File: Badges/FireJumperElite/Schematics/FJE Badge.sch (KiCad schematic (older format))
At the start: 38 parts, among them J1 USB_C_Receptacle, J2 Prog, J3 Conn_02x03_Odd_Even, J4 Conn_02x03_Odd_Even, SW1 SW_DIP_x01, SW2 SW_DIP_x01, SW3 SW_DIP_x01, U1 TLV1117-33, U2 HX4056, U3 STM32F042F6Px

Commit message: Putting stuff together
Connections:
- net at Power->1.3 (C), R3.2: now also C2.2
- net at R3.1, U1.3 (VI): no longer C2.2
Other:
- moved on the sheet: BT1, C1, C2, C3, C4, C5, C6, C7, C8, C9, D1, D10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

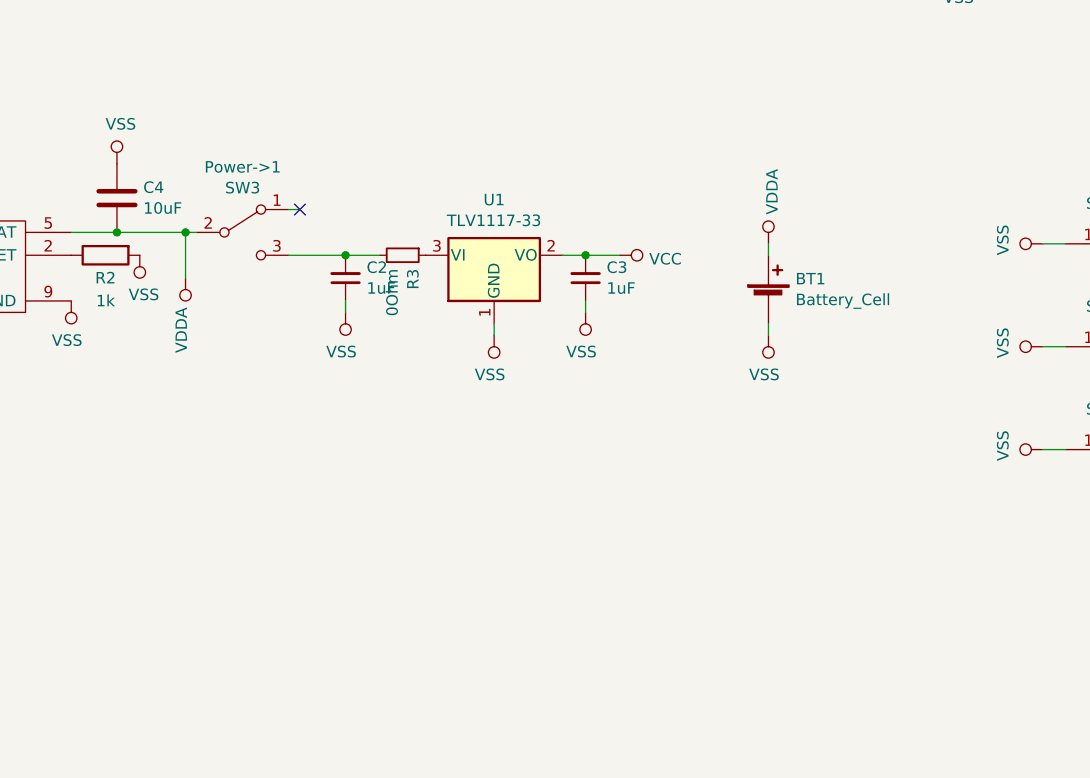
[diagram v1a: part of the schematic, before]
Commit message: FJE Badge Charlieplexing done
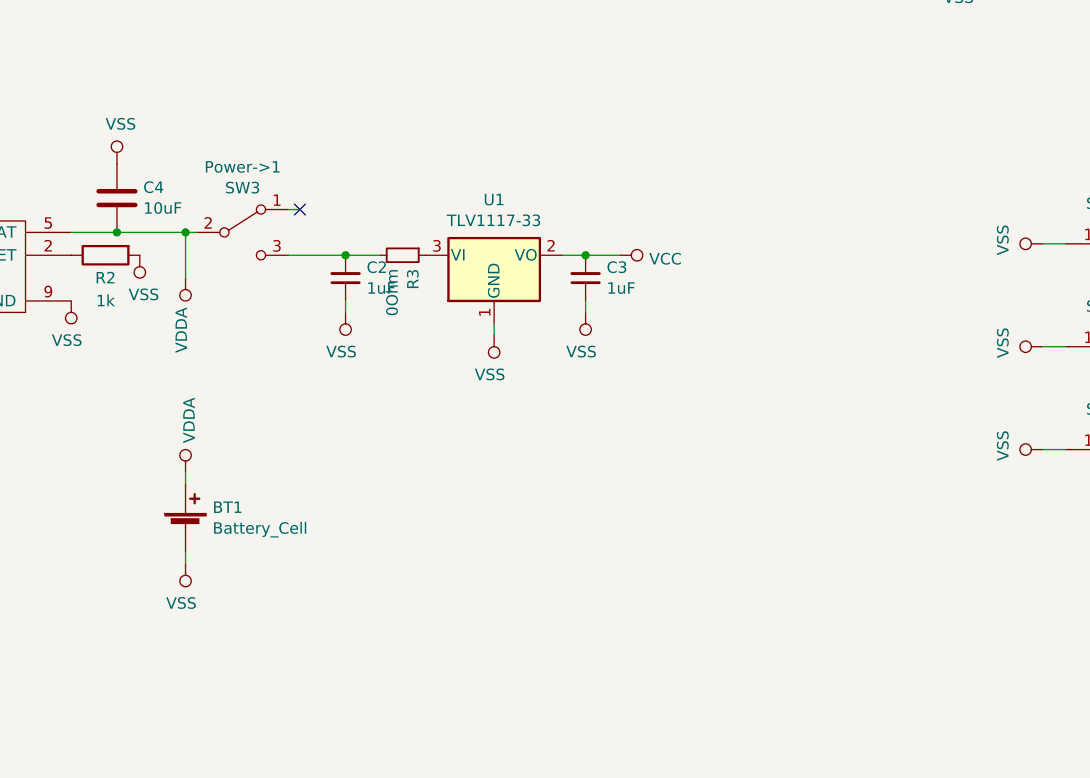
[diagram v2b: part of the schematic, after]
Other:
- moved on the sheet: BT1
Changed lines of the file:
@@
 L Device:Battery_Cell BT1
 U 1 1 5E42D738
-P 8350 5000
-F 0 "BT1" H 8468 5096 50  0000 L CNN
-F 1 "Battery_Cell" H 8468 5005 50  0000 L CNN
-F 2 "Battery:BatteryHolder_Keystone_3008_1x2450" V 8350 5060 50  0001 C CNN
-F 3 "~" V 8350 5060 50  0001 C CNN
-	1    8350 5000
+P 5800 6000
+F 0 "BT1" H 5918 6096 50  0000 L CNN
+F 1 "Battery_Cell" H 5918 6005 50  0000 L CNN
+F 2 "Battery:BatteryHolder_Keystone_3008_1x2450" V 5800 6060 50  0001 C CNN
+F 3 "~" V 5800 6060 50  0001 C CNN
+	1    5800 6000
 	1    0    0    -1
 $EndComp
@@
 L power:VDDA #PWR09
 U 1 1 5E78AC12
-P 8350 4750
-F 0 "#PWR09" H 8350 4600 50  0001 C CNN
-F 1 "VDDA" V 8367 4878 50  0000 L CNN
-F 2 "" H 8350 4750 50  0001 C CNN
-F 3 "" H 8350 4750 50  0001 C CNN
-	1    8350 4750
-	1    0    0    -1
-$EndComp
-Wire Wire Line
-	8350 4750 8350 4800
+P 5800 5750
+F 0 "#PWR09" H 5800 5600 50  0001 C CNN
+F 1 "VDDA" V 5817 5878 50  0000 L CNN
+F 2 "" H 5800 5750 50  0001 C CNN
+F 3 "" H 5800 5750 50  0001 C CNN
+	1    5800 5750
+	1    0    0    -1
+$EndComp
+Wire Wire Line
+	5800 5750 5800 5800
 $Comp
 L power:VSS #PWR010
 U 1 1 5E78E948
-P 8350 5150
-F 0 "#PWR010" H 8350 5000 50  0001 C CNN
-F 1 "VSS" H 8368 5323 50  0000 C CNN
-F 2 "" H 8350 5150 50  0001 C CNN
-F 3 "" H 8350 5150 50  0001 C CNN
-	1    8350 5150
+P 5800 6150
+F 0 "#PWR010" H 5800 6000 50  0001 C CNN
+F 1 "VSS" H 5818 6323 50  0000 C CNN
+F 2 "" H 5800 6150 50  0001 C CNN
+F 3 "" H 5800 6150 50  0001 C CNN
+	1    5800 6150
 	-1   0    0    1
 $EndComp
 Wire Wire Line
-	8350 5150 8350 5100
+	5800 6150 5800 6100
 Text GLabel 10050 2700 2    50   Input ~ 0
 Hour
